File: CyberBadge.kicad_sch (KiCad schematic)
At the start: 63 parts, among them J1 USB_C_Receptacle_USB2.0, J2 BAT_CONN, J3 Lichtenprog_conn, Q1 SS8050-G, Q2 SS8050-G, Q3 FS8205A, Q4 AO3401A, SW1 B2, SW2 B1/BOOT, SW3 SW_SPDT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

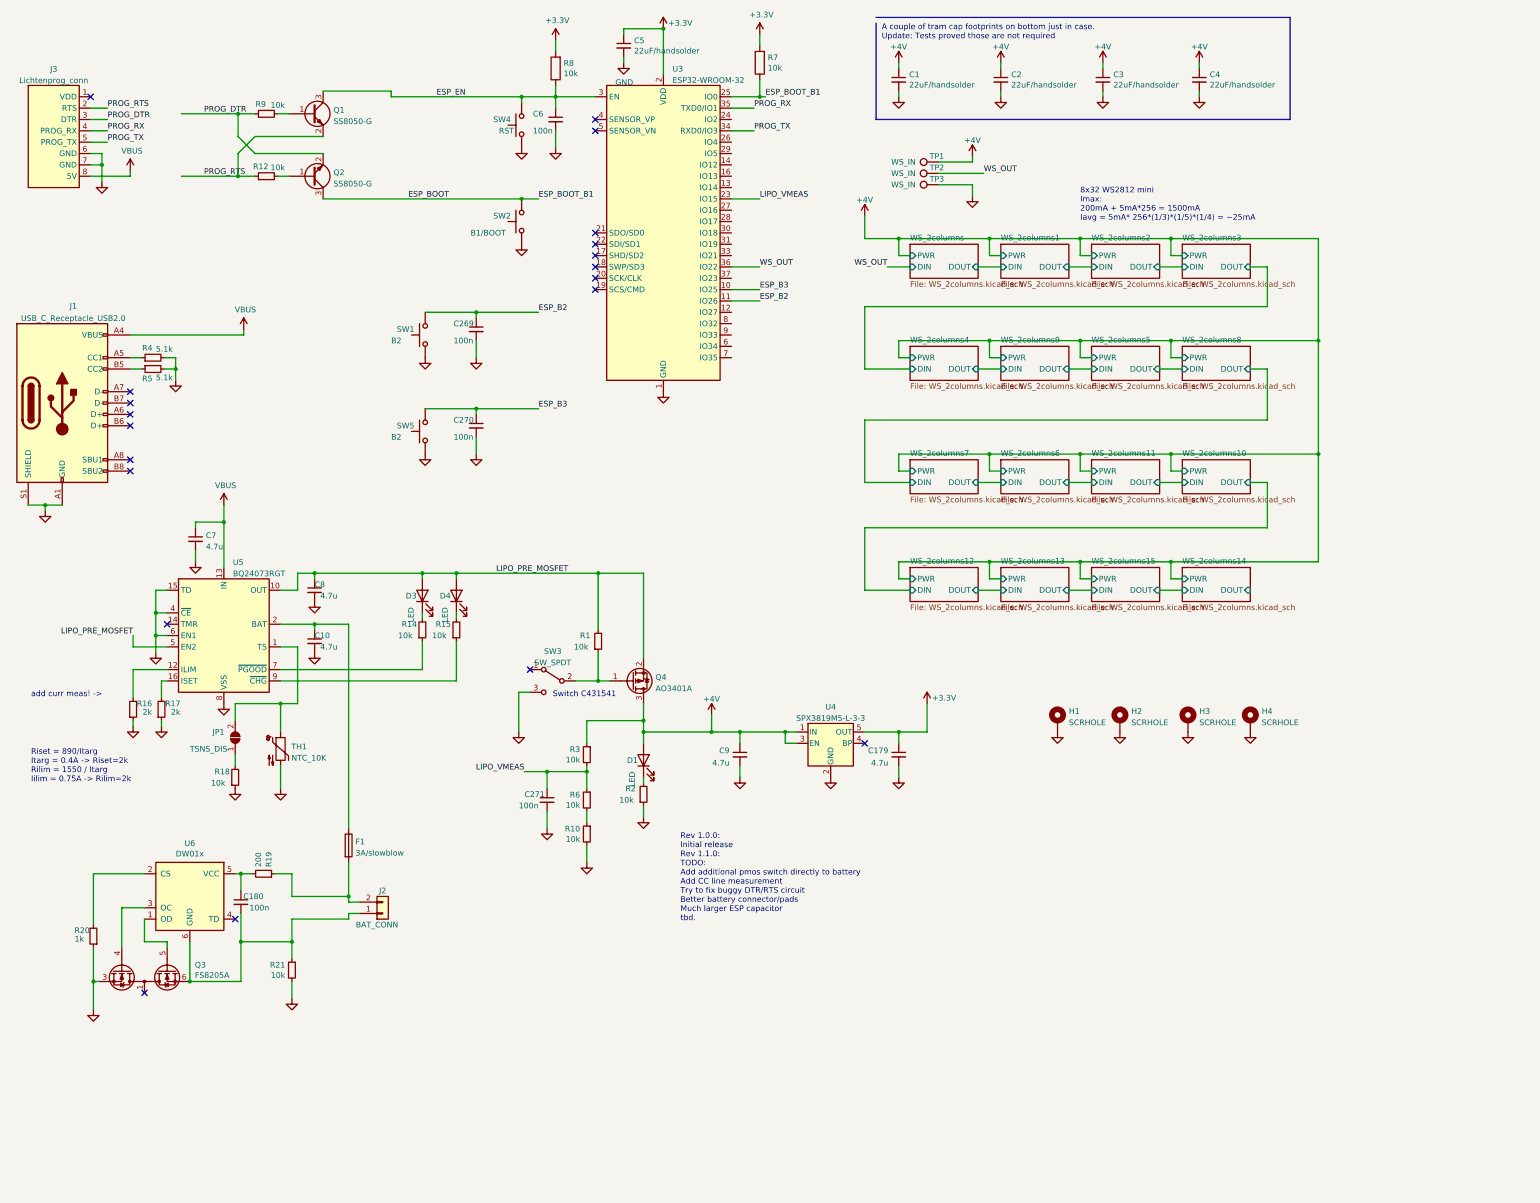
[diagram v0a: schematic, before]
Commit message: move to kicad7, tweaks for second production run
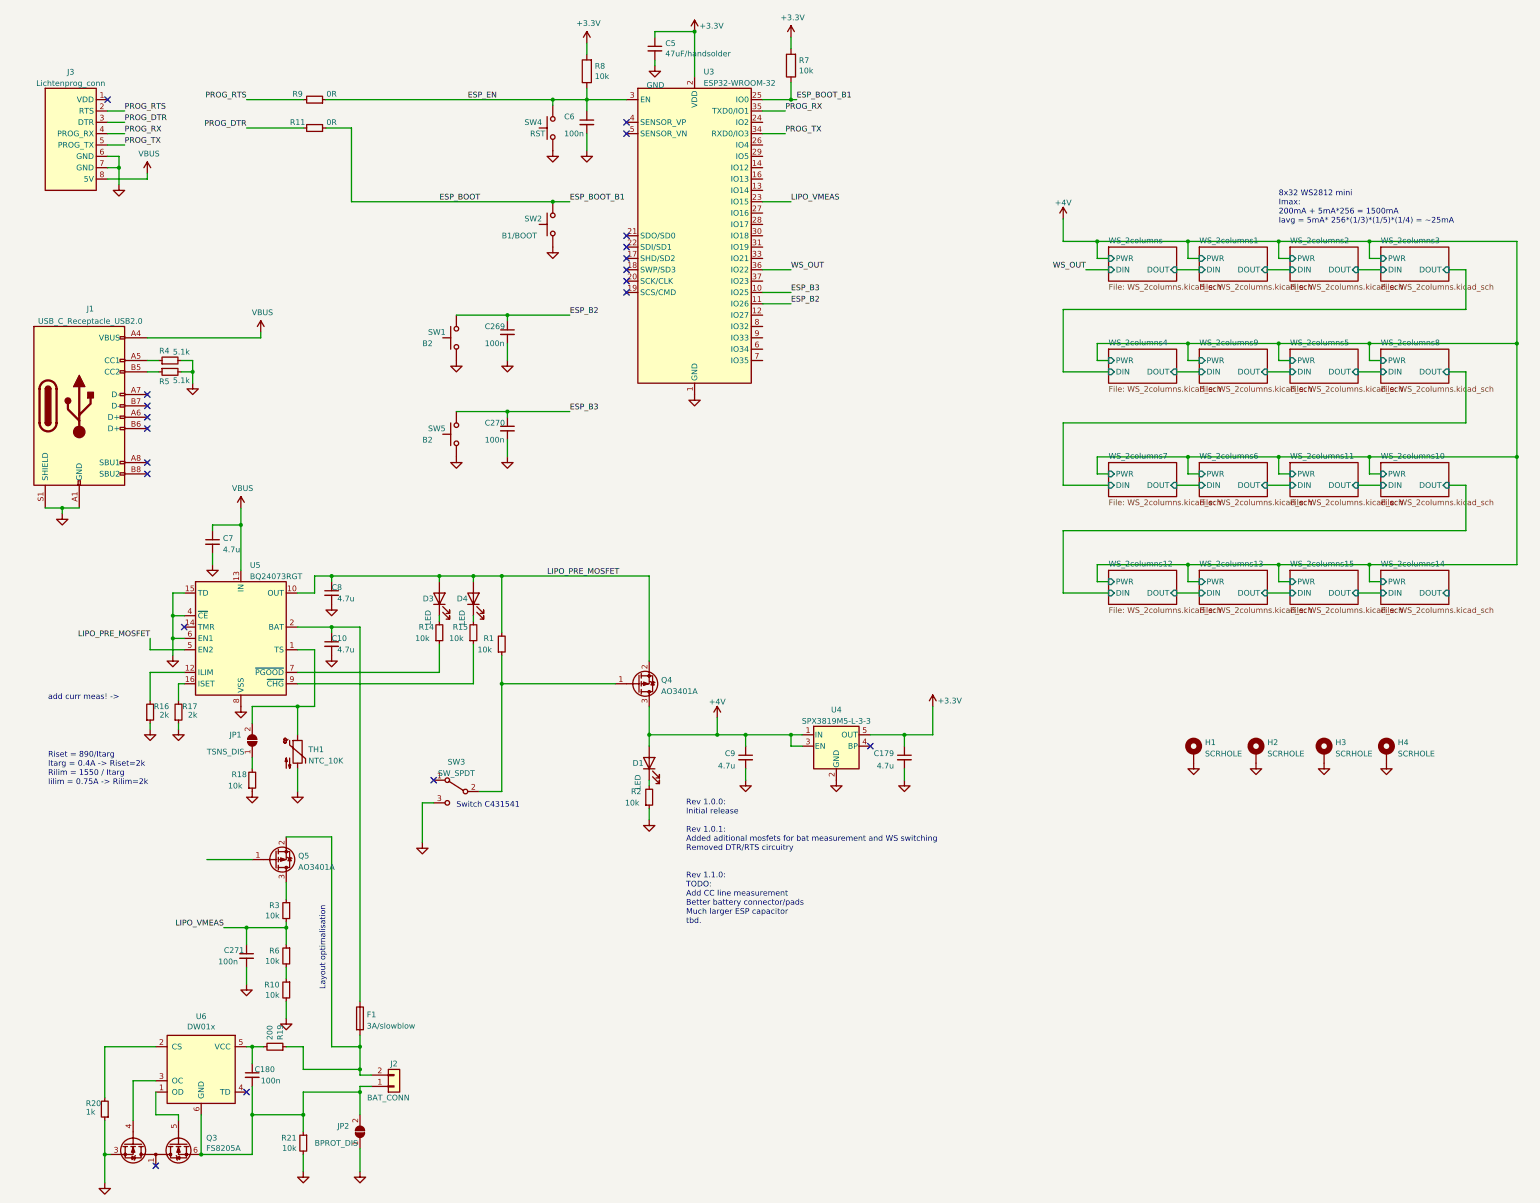
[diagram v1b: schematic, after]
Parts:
- removed C1, C2, C3, C4: 22uF/handsolder, Capacitor_SMD:C_0805_2012Metric_Pad1.18x1.45mm_HandSolder, symbol Device:C_Small
- removed Q1, Q2: SS8050-G, Package_TO_SOT_SMD:SOT-23, symbol Transistor_BJT:MMBT3904
- removed R12: 10k, Resistor_SMD:R_0201_0603Metric, symbol Device:R_Small
- removed TP1, TP2, TP3: WS_IN, TestPoint:TestPoint_Pad_D1.5mm, symbol Connector:TestPoint
- added JP2: BPROT_DIS, Jumper:SolderJumper-2_P1.3mm_Open_TrianglePad1.0x1.5mm, symbol Jumper:SolderJumper_2_Open
- added Q5: AO3401A, Package_TO_SOT_SMD:SOT-23, symbol Transistor_FET:AO3401A
- added R11: 0R, Resistor_SMD:R_0603_1608Metric_Pad0.98x0.95mm_HandSolder, symbol Device:R_Small
- C5: value 22uF/handsolder -> 47uF/handsolder; footprint Capacitor_SMD:C_0805_2012Metric_Pad1.18x1.45mm_HandSolder -> Capacitor_SMD:C_1210_3225Metric_Pad1.33x2.70mm_HandSolder
- R9: value 10k -> 0R; footprint Resistor_SMD:R_0201_0603Metric -> Resistor_SMD:R_0603_1608Metric_Pad0.98x0.95mm_HandSolder
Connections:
- net +4V: no longer R3.1
- net ESP_BOOT: now also R11.1
- net ESP_EN: now also R9.1
- net GND: now also JP2.1 (A)
- net PROG_DTR: now also R11.2; no longer R9.1
- net PROG_RTS: now also R9.2
- net at F1.2, J2.2 (Pin_2), R19.1: now also Q5.2 (S)
- net at C180.2, J2.1 (Pin_1), Q3.6 (S2)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: now also JP2.2 (B)
- new net: Q5.3 (D), R3.1
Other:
- note added: "Layout optimalisation"
- note added: "Rev 1.0.0: Initial release Rev 1.0.1: Added aditional mosfets for bat measurement and WS switching Removed DTR/RTS circuitry Rev 1.1.0: TODO: Add CC line measurement Better battery connector/pads Much larger ESP capacitor tbd."
- note removed: "A couple of tram cap footprints on bottom just in case. Update: Tests proved those are not required"
- note removed: "Rev 1.0.0: Initial release Rev 1.1.0: TODO: Add additional pmos switch directly to battery Add CC line measurement Try to fix buggy DTR/RTS circuit Better battery connector/pads Much larger ESP capacitor tbd."
- moved on the sheet: C10, C179, C180, C269, C270, C5, C6, C7, C8, C9, D1, D3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
